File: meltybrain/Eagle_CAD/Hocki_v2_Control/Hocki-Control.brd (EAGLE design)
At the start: 90 x 46 mm, 154 parts, among them J1 SM03B-SRSS-TB(LF)(SN), J2 SM04B-SRSS-TB(LF)(SN), J3 SM02B-SRSS-TB(LF)(SN), J4 SM04B-SRSS-TB(LF)(SN), J5 SM03B-SRSS-TB(LF)(SN), J6 SM03B-SRSS-TB(LF)(SN), U1 AP63200, U10 LMH6612MAX/NOPB, U11 TLV3502AIDCNR, U12 LMH6612MAX/NOPB, U13 TMP235A4DCKR, U14 ADXL375, U15 NL27WZ32USG, U16 ADXL375, U17 ADXL375, U18 NL27WZ32USG, U19 ADXL375, U2 TEENSY_4.1, U20 LMV358, U21 LMV358, U22 HMC1052L-TR, U23 LMV358, U24 IRF7509, U3 AP2210K-5.0TRG1, U4 AP2210K-3.3TRG1, U5 74AHC1G04GW,125, U6 LDL212PU50R, U7 LMH6612MAX/NOPB, U8 LMH6612MAX/NOPB, U9 TMUX1219DCKR

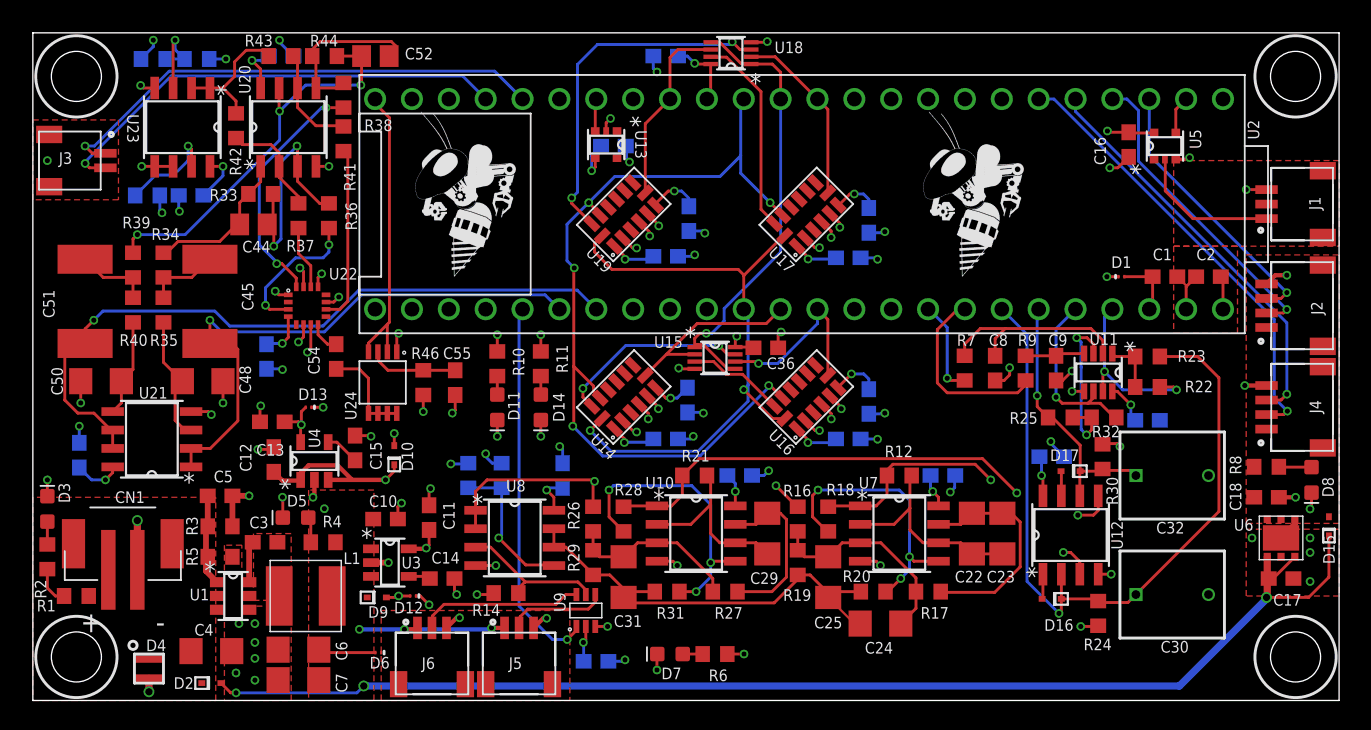
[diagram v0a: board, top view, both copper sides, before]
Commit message: Moving v2 to a new directory to avoid merge conflicts and allow both versions to coexist in master
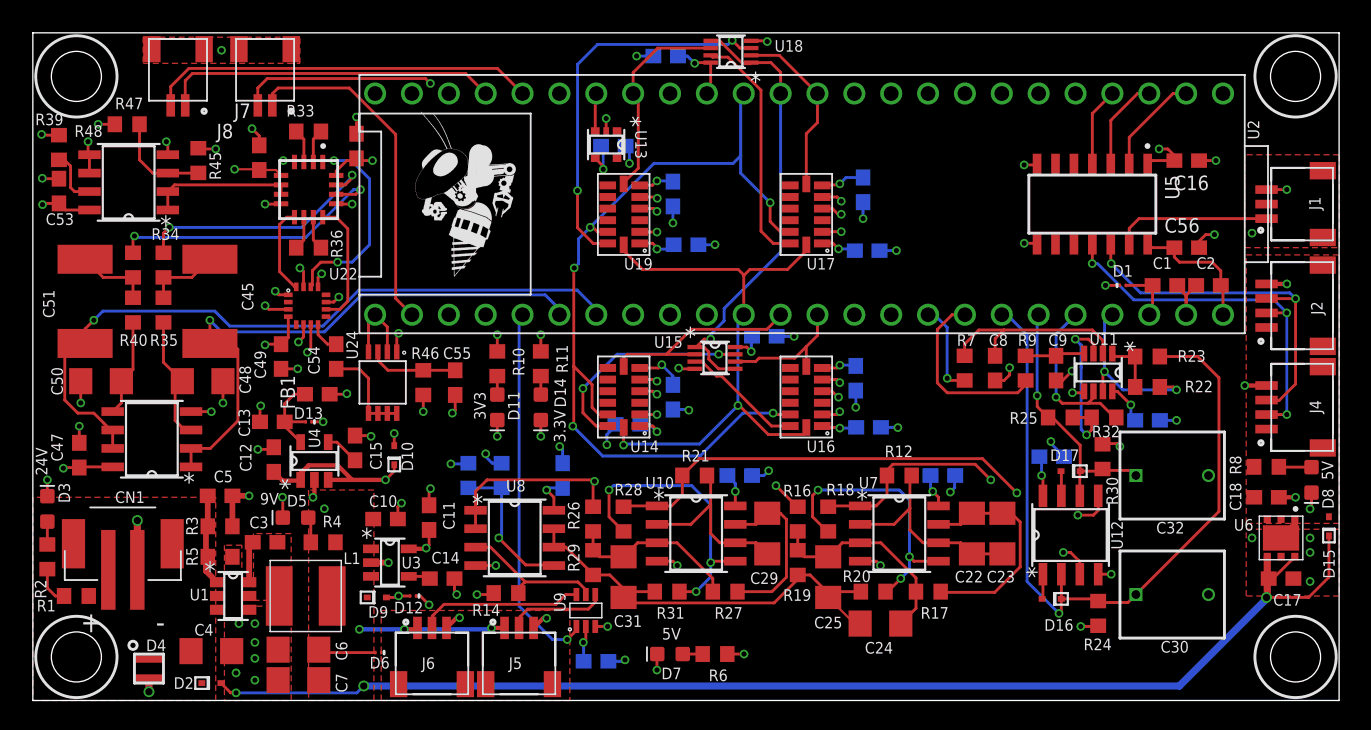
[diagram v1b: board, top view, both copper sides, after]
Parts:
- removed C52: 1000pF, rcl:C0805
- removed J3: SM02B-SRSS-TB(LF)(SN), Hocki_Library:SM02B-SRSS-TB(LF)(SN)
- removed R37, R38, R41: 4.99k, rcl:R0603
- removed R42, R43, R44: 499k, rcl:R0603
- removed U$1: (no value), RoboJackets-Aesthetics:ROBOBUZZ_0.6X
- added C56: 0.1uF, rcl:C0603
- added FB1: MPZ1608R391ATD25, Hocki_Library:0603
- added J7, J8: SM02B-SRSS-TB(LF)(SN), Hocki_Library:SM02B-SRSS-TB(LF)(SN)
- C44: value 1000pF -> 0.1uF; device rcl:C0805 -> rcl:C0603
- CN1: value (none) -> JST_2PIN
- R33: value 499k -> 49.9
- R36: value 4.99k -> 49.9
- U20: value LMV358 -> AD8426ACPZ-WP; device Hocki_Library:8-SOIC -> Hocki_Library:16LFCSP
- U21, U23: value LMV358 -> LMH6612MAX/NOPB
- U5: value 74AHC1G04GW,125 -> TXS0104ED; device Hocki_Library:SOT-353 -> Hocki_Library:14-SOIC
- moved C53 9.10 mm to (-50.2, 7.90), flipped to the top, turned to 90 degrees
- moved C46 8.09 mm to (-29.7, 11.0), flipped to the top, turned to 90 degrees
- moved R45 7.00 mm to (-40.6, 10.0), flipped to the top, turned to 270 degrees
- moved R48 6.94 mm to (-50.2, 10.9), flipped to the top, turned to 90 degrees
- moved U5 6.40 mm to (21.0, 7.00), turned to 270 degrees
- moved R33 5.42 mm to (-33.0, 12.0), turned to 180 degrees
- moved U23 5.30 mm to (-45.4, 8.50), turned to 180 degrees
- moved R47 4.85 mm to (-45.5, 12.5), flipped to the top, turned to 180 degrees
- moved C44 4.62 mm to (-36.4, 10.2), turned to 90 degrees
- moved U20 4.52 mm to (-33.0, 8.00), turned to 270 degrees
- moved C16 4.15 mm to (27.5, 10.0), turned to 0 degrees
- moved C34 2.79 mm to (-11.0, -8.18), turned to 0 degrees
- moved R36 2.61 mm to (-33.0, 4.00), turned to 180 degrees
- moved C41 2.14 mm to (5.20, 7.98)
- moved C43 2.02 mm to (-7.90, 7.70)
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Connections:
- removed net LED_CLK1: J2.2, U2.2
- removed net LED_DATA1: J2.3, U2.1
- removed net MAG_OUTPUTA: C44.2, R33.1, R34.2, U20.1
- removed net MAG_OUTPUTB: C52.2, R39.2, R44.1, U20.7
- removed net OUT+(A): R36.2, U22.3
- removed net OUT+(B): R38.2, U22.16
- removed net OUT-(A): R37.2, U22.14
- removed net OUT-(B): R41.2, U22.10
- removed net RC_SIGNAL: J1.1, U5.2
- removed net SBUS: U2.0, U5.4
- new net 3V3_LED_CLK: U2.2, U5.4
- new net 3V3_LED_DATA: U2.1, U5.3
- new net 3V3_RC_SIGNAL: U2.0, U5.2
- new net 5V_LED_CLK: J2.2, J4.2, U5.11
- new net 5V_LED_DATA: J2.3, J4.3, U5.12
- new net 5V_RC_SIGNAL: J1.1, U5.13
- new net ESC_TEL_L: J8.2, U2.28
- new net ESC_TEL_R: J7.1, U2.34
- new net N$28: C13.1, D13.C2, FB1.1, U4.5
- new net N$31: U20.4, U22.3
- new net N$32: U20.1, U22.14
- new net N$33: U20.9, U22.16
- new net N$38: R33.1, U20.2
- new net N$39: R36.2, U20.10
- new net N$40: R36.1, U20.11
- net +3V3: now also C44.1, FB1.2, U20.16, U20.5; no longer C13.1, D13.C2, U20.8, U4.5
- net 3.3V: now also U5.1, U5.8; no longer U5.5
- net 5V: now also C56.1, U5.14
- net CS4: now also U2.25; no longer U2.24
- net ESC_L: now also J8.1, U2.29; no longer J3.1, U2.28
- net ESC_R: now also J7.2, U2.24; no longer J3.2, U2.29
- net GND: now also C44.2, C56.2, J7.S1, J7.S2, J8.S1, J8.S2, U20.13, U20.8, U5.7; no longer J3.S1, J3.S2, U20.4, U5.3
- net LED_CLK2: now also U2.3; no longer J4.2, U2.4
- net LED_DATA2: now also U2.4; no longer J4.3, U2.3
- net N$34: now also U20.12, U22.10; no longer R41.1, R43.1, U20.6
- net N$35: now also R39.2, U20.14; no longer C52.1, R38.1, R44.2, U20.5
- net N$36: now also R34.2, U20.15; no longer R37.1, R42.1, U20.2
- net N$37: no longer C44.1, R36.1
- net S/R: now also U2.33; no longer U2.32
- net VREF/2: now also U20.6, U20.7; no longer R42.2, R43.2
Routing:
- net LED_CLK2: track 30.8 -> 0.00 mm, vias 1 -> 0
- net LED_DATA2: track 27.9 -> 0.00 mm, vias 1 -> 0
- net MAG_OUTPUTB: track 27.5 -> 0.00 mm, vias 3 -> 0
- net ESC_TEL_L: track 0.00 -> 26.8 mm
- net 5V_LED_CLK: track 0.00 -> 26.0 mm, vias 0 -> 3
- net 5V_LED_DATA: track 0.00 -> 25.5 mm, vias 0 -> 2
- net ESC_TEL_R: track 0.00 -> 23.7 mm
- net LED_CLK1: track 21.6 -> 0.00 mm, vias 1 -> 0
- net LED_DATA1: track 18.8 -> 0.00 mm, vias 1 -> 0
- net OUT+(B): track 16.9 -> 0.00 mm, vias 2 -> 0
- net S/R: track 20.3 -> 5.66 mm
- net N$37: track 16.8 -> 2.32 mm, vias 2 -> 0
- net 5V: track 30.9 -> 45.1 mm, vias 9 -> 10
- net N$32: track 0.00 -> 14.2 mm, vias 0 -> 2
- net N$31: track 0.00 -> 13.0 mm, vias 0 -> 2
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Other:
- board text added: "24V"
- board text added: "3.3V"
- board text added: "3V3"
- board text added: "5V"
- board text added: "9V"
- board text added: "Hocki Control V2"
- board text removed: "Hocki Control V1"
